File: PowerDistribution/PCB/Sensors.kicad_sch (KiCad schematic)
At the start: 11 parts, among them IC4 LM75BDP,118, IC5 INA219AIDR, IC6 ADS1015BQDGSRQ1

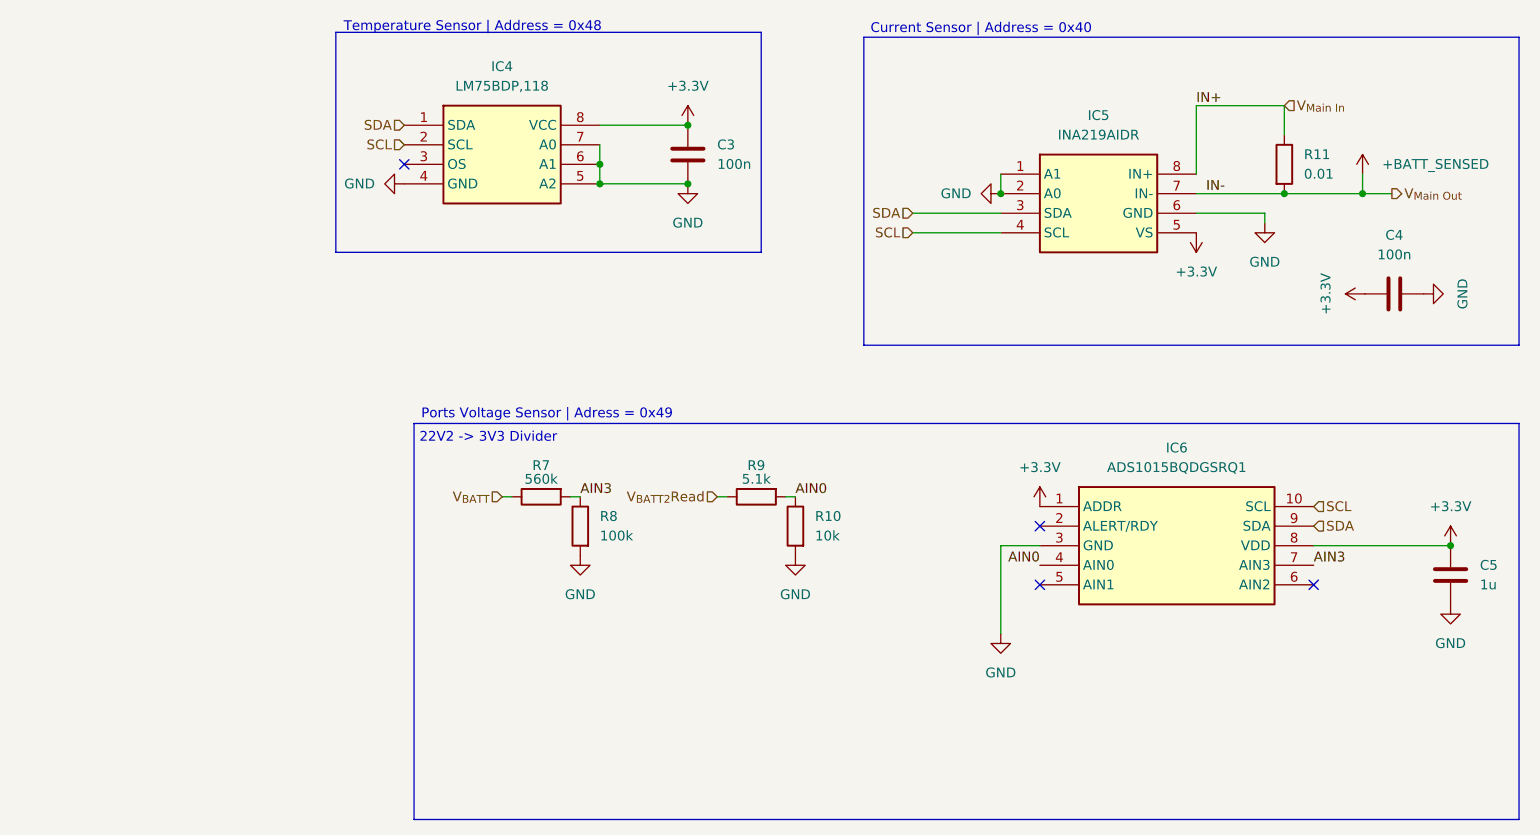
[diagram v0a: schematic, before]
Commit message: Firmware for v2.0, and hardware fixes change for v2.1
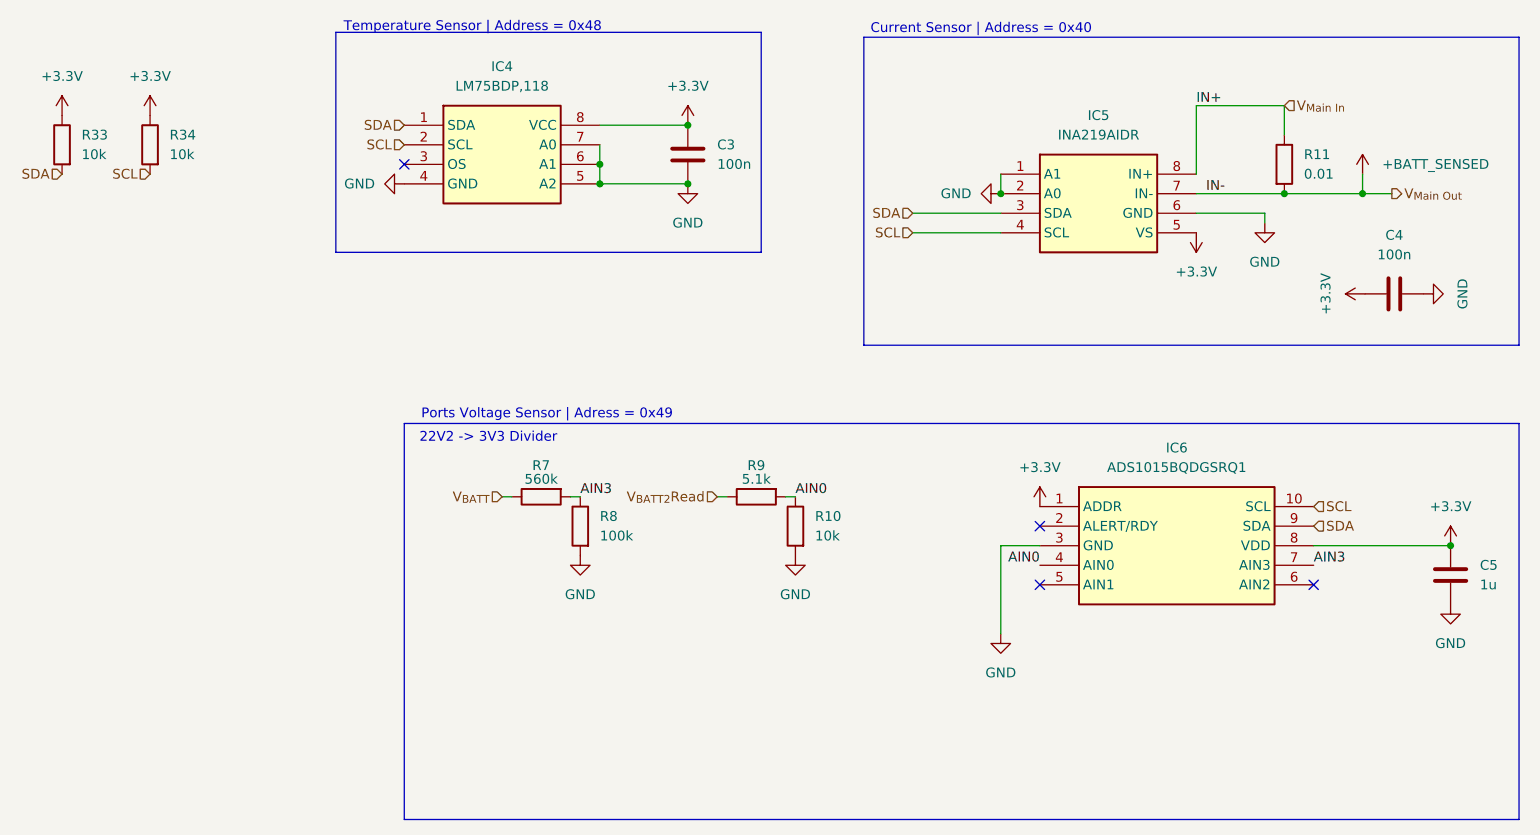
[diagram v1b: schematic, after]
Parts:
- added R33, R34: 10k, Resistor_SMD:R_0402_1005Metric, symbol Device:R
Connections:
- net +3.3V: now also R33.1, R34.1
- net SCL: now also R34.2
- net SDA: now also R33.2

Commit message: Gitignore fix
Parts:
- IC4: footprint SOP65P490X110-8N -> Footprints:LM75BDP,118
- IC5: footprint SOIC127P600X175-8N -> Footprints:INA219AIDR
- IC6: footprint Footprints:SOP50P490X110-10N -> Footprints:ADS1015BQDGSRQ1
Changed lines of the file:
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@@
 			)
 		)
-		(property "Footprint" "Footprints:SOP50P490X110-10N"
+		(property "Footprint" "Footprints:ADS1015BQDGSRQ1"
 			(at 208.28 182.55 0)
 			(hide yes)
@@
 			)
 		)
-		(property "Footprint" "SOIC127P600X175-8N"
+		(property "Footprint" "Footprints:INA219AIDR"
 			(at 193.04 139.37 0)
 			(hide yes)
@@
 			)
 		)
-		(property "Footprint" "SOP65P490X110-8N"
+		(property "Footprint" "Footprints:LM75BDP,118"
 			(at 115.57 133.02 0)
 			(hide yes)
